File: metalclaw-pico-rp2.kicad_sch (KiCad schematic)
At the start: 124 parts, among them J1 USB4105-GF-A, J2 FTSH-105-01-L-DV-K, SW1 PTS810SJM250SMTR LFS, SW2 PTS810SJM250SMTR LFS, U1 XC6220B331MR-G, U2 RP2354B, U3 APS6404L-3SQR-SN, Y1 ABM8-272-T3

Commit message: Add test points for usb and debugger
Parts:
- added TP1, TP2, TP3, TP4, TP5, TP6, TP7, TP8: TestPoint, TestPoint:TestPoint_Pad_D1.0mm, symbol Connector:TestPoint
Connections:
- net +3V3: now also TP5.1
- net BOOTSEL: now also TP8.1
- net GND: now also TP6.1
- net RESET: now also TP7.1
- net USB_D+: now also TP2.1
- net USB_D-: now also TP1.1
- net at J2.4 (Pin_4), U2.33 (SWCLK): now also TP3.1
- net at J2.2 (Pin_2), U2.34 (SWDIO): now also TP4.1

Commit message: Fix cap value
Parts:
- C11: value 1u -> 4.7u; LCSC C52923 -> C326586; LCSC MPN CL05A105KA5NQNC -> CC0402KRX5R6BB475; Mouser 810-C1005X7S1A105K -> 810-C1005X5R0J475K
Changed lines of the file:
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@@
 			)
 		)
-		(property "Value" "1u"
+		(property "Value" "4.7u"
 			(at 179.578 73.66 90)
 			(effects
@@
 			)
 		)
-		(property "Datasheet" "https://eu.mouser.com/en/ProductDetail/TDK/C1005X7S1A105K050BC"
+		(property "Datasheet" "https://product.tdk.com/en/search/capacitor/ceramic/mlcc/info?part_no=C1005X5R0J475K050BC"
 			(at 177.8 78.74 0)
 			(effects
@@
 			)
 		)
-		(property "Description" "1 uF +/-10% 10 V X7S 0402 carrier MCU decoupling capacitor, TDK C1005X7S1A105K050BC"
+		(property "Description" "4.7 uF 6.3 V X5R +/-10% 0402 regulator input capacitor (CIN), TDK C1005X5R0J475K050BC"
 			(at 177.8 78.74 0)
 			(effects
@@
 			)
 		)
-		(property "Mouser" "810-C1005X7S1A105K"
+		(property "Mouser" "810-C1005X5R0J475K"
 			(at 177.8 78.74 90)
 			(effects
@@
 			)
 		)
-		(property "LCSC" "C52923"
+		(property "LCSC" "C326586"
 			(at 177.8 78.74 90)
 			(effects
@@
 			)
 		)
-		(property "LCSC MPN" "CL05A105KA5NQNC"
+		(property "LCSC MPN" "CC0402KRX5R6BB475"
 			(at 177.8 78.74 90)
 			(effects

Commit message: Update JLCPCB component sourcing and fabrication package
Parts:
- C1, C2: Manufacturer (none) -> Samsung Electro-Mechanics; Mouser 810-C1608X7R1A106M08 -> (none)
- C10, C11, C12, C13, C24: Manufacturer (none) -> Yageo; Mouser 810-C1005X5R0J475K -> (none)
- C14, C15, C16, C17, C18, C19, C20, C21, C22, C23, C25, C29, C3: Manufacturer (none) -> Yageo; Mouser 581-KGM03BR71A104KH -> (none)
- C28: Manufacturer (none) -> Samsung Electro-Mechanics; Mouser 810-C1005X7S1A105K -> (none)
- D1: value CUHS20F30,H3F -> SS14HE; footprint MetalClaw:D_US2H_CUHS20F30 -> MetalClaw:D_SOD-323HE_SS14HE; LCSC C5357828 -> C28646397; MPN (none) -> SS14HE; Manufacturer (none) -> TECH PUBLIC; Mouser 757-CUHS20F30H3F -> (none)
- J1: value USB4105-GF-A -> HH 16P TYPE-C (Y495); footprint MetalClaw:USB_C_Receptacle_GCT_USB4105-xx-A_16P_TopMnt_Horizontal -> MetalClaw:USB_C_Receptacle_HH_Y495_16P_TopMnt_Horizontal; LCSC C3020560 -> C52209111; MPN USB4105-GF-A -> HH 16P TYPE-C (Y495); Manufacturer GCT -> HH; Mouser 640-USB4105-GF-A -> (none); Supplier (none) -> JLCPCB/LCSC
- SW1, SW2: value PTS810SJM250SMTR LFS -> YTS810SJM; LCSC C116501 -> C2910643; MPN (none) -> YTS810SJM; Manufacturer (none) -> YIYUAN; Mouser 611-PTS810SJM250SMTR -> (none)
- U3: MPN (none) -> APS6404L-3SQR-SN; Manufacturer (none) -> AP Memory; Mouser 878-APS6404L-3SQR-SN -> (none)

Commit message: Correct assembly footprints and prepare JLCPCB manufacturing package
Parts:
- J2: footprint Connector_PinHeader_1.27mm:PinHeader_2x05_P1.27mm_Vertical_SMD -> MetalClaw:Samtec_FTSH-105-01-L-DV-K
- L1: footprint Inductor_SMD_Wurth:L_Wurth_WE-LQSH-2010 -> MetalClaw:L_Abracon_AOTA-B201610S3R3-101-T
- U2: footprint Package_DFN_QFN:QFN-80-1EP_10x10mm_P0.4mm_EP3.4x3.4mm -> MetalClaw:QFN-80_RP2354B_10x10mm_P0.4mm_EP3.4mm_ViaAwarePaste
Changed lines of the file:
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@@
 			)
 		)
-		(property "Footprint" "Package_DFN_QFN:QFN-80-1EP_10x10mm_P0.4mm_EP3.4x3.4mm"
+		(property "Footprint" "MetalClaw:QFN-80_RP2354B_10x10mm_P0.4mm_EP3.4mm_ViaAwarePaste"
 			(at 295.91 146.05 0)
 			(effects
@@
 			)
 		)
-		(property "Footprint" "Inductor_SMD_Wurth:L_Wurth_WE-LQSH-2010"
+		(property "Footprint" "MetalClaw:L_Abracon_AOTA-B201610S3R3-101-T"
 			(at 290.83 80.01 0)
 			(effects
@@
 			)
 		)
-		(property "Footprint" "Connector_PinHeader_1.27mm:PinHeader_2x05_P1.27mm_Vertical_SMD"
+		(property "Footprint" "MetalClaw:Samtec_FTSH-105-01-L-DV-K"
 			(at 375.92 187.96 0)
 			(effects

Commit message: Prepare v1.r1 documentation and release workflow
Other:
- title: (none) -> MetalClaw Pico RP2
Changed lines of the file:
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@@
 	(generator_version "9.0")
 	(paper "B")
+	(title_block
+		(title "MetalClaw Pico RP2")
+		(date "2026-10-24")
+		(rev "v1.r1")
+		(comment 1 "Author: Renz Bagaporo")
+	)
 	(junction
 		(at 252.73 97.79)

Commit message: Select compact keyed Samtec SWD header for JLCPCB assembly
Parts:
- J2: value FTSH-105-01-L-DV-K -> FTSH-105-01-L-DV-K-P-TR; LCSC C5155080 -> C2932107; MPN FTSH-105-01-L-DV-K -> FTSH-105-01-L-DV-K-P-TR; Mouser 200-FTSH10501LDVK -> (none)
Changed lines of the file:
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@@
 			)
 		)
-		(property "Value" "FTSH-105-01-L-DV-K"
+		(property "Value" "FTSH-105-01-L-DV-K-P-TR"
 			(at 377.19 198.628 0)
 			(effects
@@
 			)
 		)
-		(property "Datasheet" "https://www.samtec.com/products/ftsh-105-01-l-dv-k"
+		(property "Datasheet" "https://suddendocs.samtec.com/prints/ftsh-1xx-xx-xxx-dv-xxx-xxx-mkt.pdf"
 			(at 375.92 187.96 0)
 			(effects
@@
 			)
 		)
-		(property "Description" "10-pin 2-row 1.27 mm vertical SMT micro header with keying notch for SWD, Samtec FTSH-105-01-L-DV-K"
+		(property "Description" "10-pin 2-row 1.27 mm vertical SMT SWD header with compact plastic key, 3.05 mm mating posts, 10 microinch gold / matte tin, pick-and-place pad, tape and reel; Samtec FTSH-105-01-L-DV-K-P-TR"
 			(at 375.92 187.96 0)
 			(effects
@@
 			)
 		)
-		(property "MPN" "FTSH-105-01-L-DV-K"
+		(property "MPN" "FTSH-105-01-L-DV-K-P-TR"
 			(at 375.92 187.96 0)
 			(effects
@@
 			)
 		)
-		(property "Mouser" "200-FTSH10501LDVK"
+		(property "Mouser" ""
 			(at 375.92 187.96 0)
 			(effects
@@
 			)
 		)
-		(property "LCSC" "C5155080"
+		(property "LCSC" "C2932107"
 			(at 375.92 187.96 0)
 			(effects

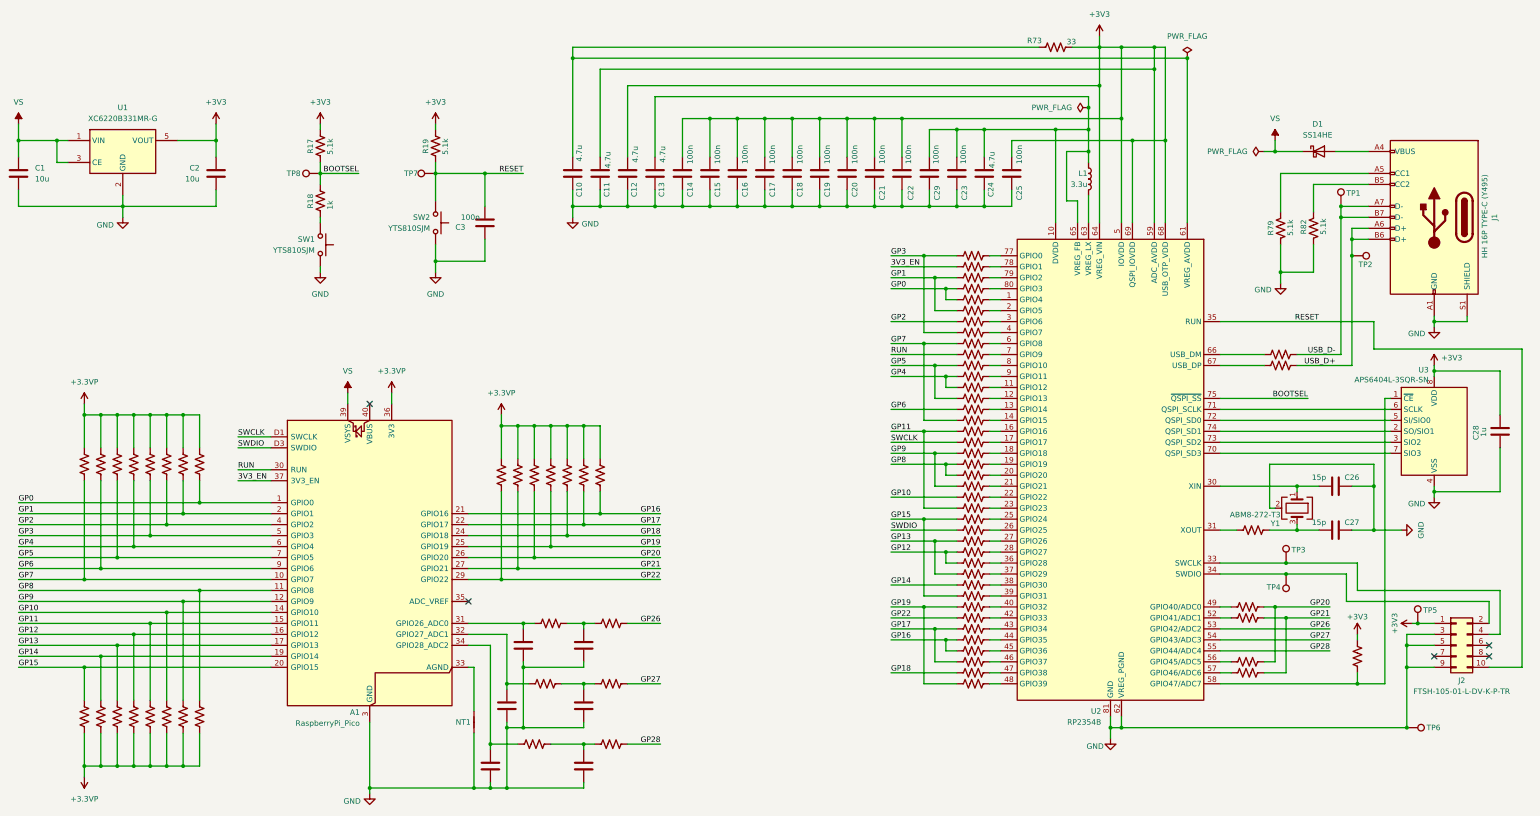
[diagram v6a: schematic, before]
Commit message: Reduce assembly BOM cost and add unshrouded SWD orientation outline
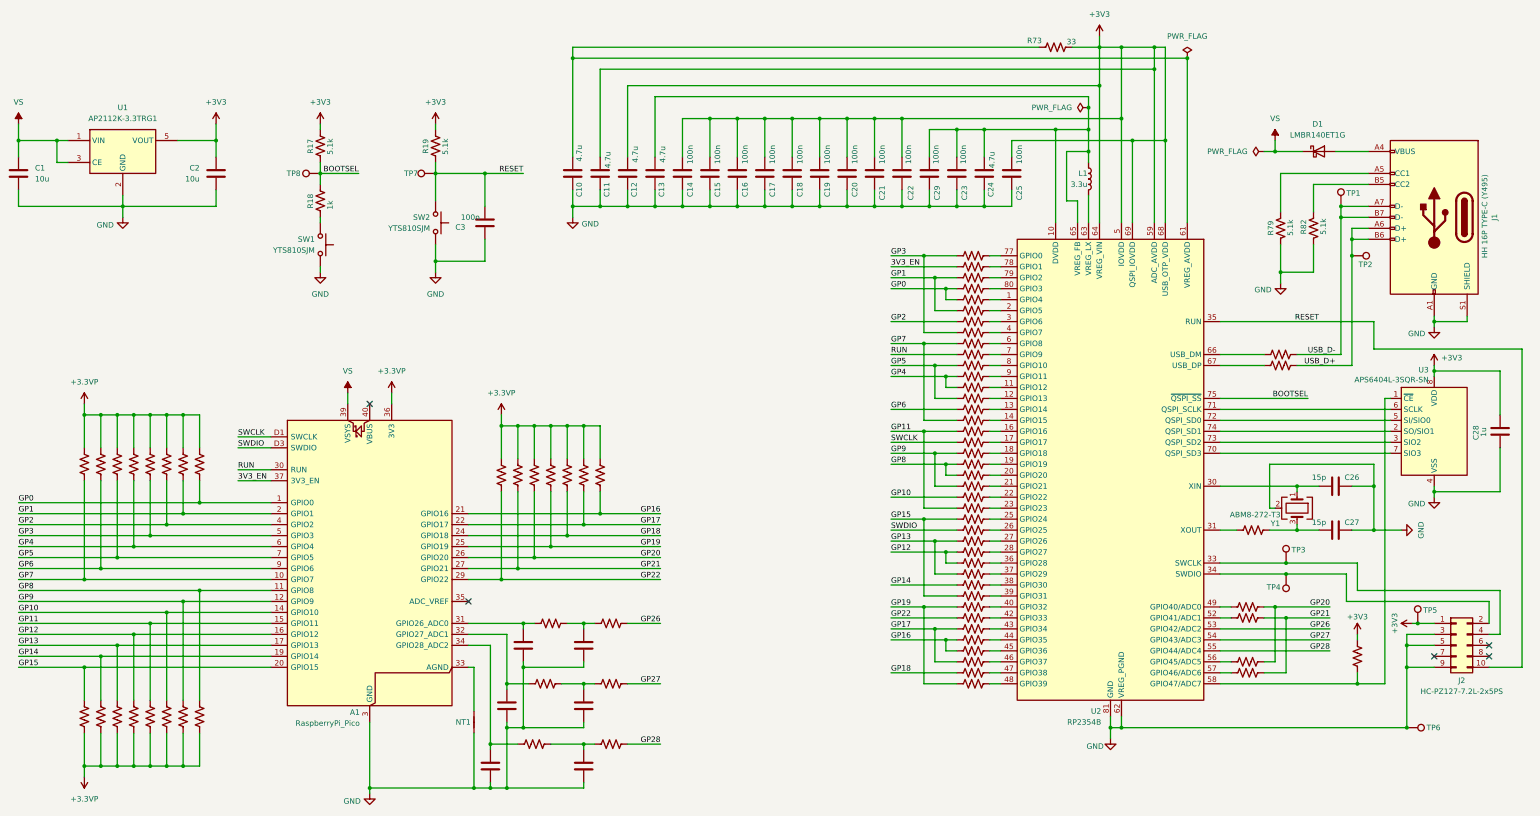
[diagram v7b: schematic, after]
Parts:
- D1: value SS14HE -> LMBR140ET1G; LCSC C28646397 -> C172430; MPN SS14HE -> LMBR140ET1G; Manufacturer TECH PUBLIC -> LRC
- J2: value FTSH-105-01-L-DV-K-P-TR -> HC-PZ127-7.2L-2x5PS; footprint MetalClaw:Samtec_FTSH-105-01-L-DV-K -> MetalClaw:HCTL_HC-PZ127-7.2L-2x5PS; LCSC C2932107 -> C27985146; MPN FTSH-105-01-L-DV-K-P-TR -> HC-PZ127-7.2L-2x5PS; Manufacturer Samtec -> HCTL
- U1: value XC6220B331MR-G -> AP2112K-3.3TRG1; LCSC C86534 -> C51118; MPN (none) -> AP2112K-3.3TRG1; Manufacturer (none) -> Diodes Incorporated; Mouser 865-XC6220B331MR-G -> (none)
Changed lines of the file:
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@@
 			)
 		)
-		(property "Value" "XC6220B331MR-G"
+		(property "Value" "AP2112K-3.3TRG1"
 			(at 67.31 66.04 0)
 			(effects
@@
 			)
 		)
-		(property "Datasheet" "https://www.torexsemi.com/file/xc6220/XC6220.pdf"
+		(property "Datasheet" "https://www.diodes.com/datasheet/download/AP2112.pdf"
 			(at 86.36 99.06 0)
 			(effects
@@
 			)
 		)
-		(property "Description" "1 A low-dropout regulator, fixed 3.3 V output, SOT-25, Torex XC6220B331MR-G"
+		(property "Description" "600 mA fixed 3.3 V low-dropout regulator, SOT-25, active-high enable; Diodes Incorporated AP2112K-3.3TRG1"
 			(at 67.31 73.66 0)
 			(effects
@@
 			)
 		)
-		(property "Mouser" "865-XC6220B331MR-G"
+		(property "Mouser" ""
+			(at 67.31 73.66 0)
+			(effects
+				(font
+					(size 1.27 1.27)
+				)
+				(hide yes)
+			)
+		)
+		(property "Manufacturer" "Diodes Incorporated"
+			(at 67.31 73.66 0)
+			(effects
+				(font
+					(size 1.27 1.27)
+				)
+				(hide yes)
+			)
+		)
+		(property "MPN" "AP2112K-3.3TRG1"
 			(at 67.31 73.66 0)
 			(effects
@@
 			)
 		)
-		(property "LCSC" "C86534"
+		(property "LCSC" "C51118"
 			(at 67.31 73.66 0)
 			(effects
@@
 			)
 		)
-		(property "Value" "FTSH-105-01-L-DV-K-P-TR"
+		(property "Value" "HC-PZ127-7.2L-2x5PS"
 			(at 377.19 198.628 0)
 			(effects
@@
 			)
 		)
-		(property "Footprint" "MetalClaw:Samtec_FTSH-105-01-L-DV-K"
+		(property "Footprint" "MetalClaw:HCTL_HC-PZ127-7.2L-2x5PS"
 			(at 375.92 187.96 0)
 			(effects
@@
 			)
 		)
-		(property "Datasheet" "https://suddendocs.samtec.com/prints/ftsh-1xx-xx-xxx-dv-xxx-xxx-mkt.pdf"
+		(property "Datasheet" "https://datasheet.lcsc.com/datasheet/pdf/6cceb9a5157e418f0d202dde8ff2fbeb.pdf?productCode=C27985146"
 			(at 375.92 187.96 0)
 			(effects
@@
 			)
 		)
-		(property "Description" "10-pin 2-row 1.27 mm vertical SMT SWD header with compact plastic key, 3.05 mm mating posts, 10 microinch gold / matte tin, pick-and-place pad, tape and reel; Samtec FTSH-105-01-L-DV-K-P-TR"
+		(property "Description" "10-pin 2-row 1.27 mm vertical SMT unshrouded header, 0.40 mm square contacts, 4.0 mm mating posts; HCTL HC-PZ127-7.2L-2x5PS"
 			(at 375.92 187.96 0)
 			(effects
@@
 			)
 		)
-		(property "Manufacturer" "Samtec"
+		(property "Manufacturer" "HCTL"
 			(at 375.92 187.96 0)
 			(effects
@@
 			)
 		)
-		(property "MPN" "FTSH-105-01-L-DV-K-P-TR"
+		(property "MPN" "HC-PZ127-7.2L-2x5PS"
 			(at 375.92 187.96 0)
 			(effects
@@
 			)
 		)
-		(property "LCSC" "C2932107"
+		(property "LCSC" "C27985146"
 			(at 375.92 187.96 0)
 			(effects
@@
 			)
 		)
-		(property "Value" "SS14HE"
+		(property "Value" "LMBR140ET1G"
 			(at 343.8525 69.85 0)
 			(effects
@@
 			)
 		)
-		(property "Datasheet" "https://datasheet.lcsc.com/datasheet/pdf/6c23897d9338a6092c7736bca8f498a2.pdf?productCode=C28646397"
+		(property "Datasheet" "https://www.lrc.cn/Upload/PDF/Product/SBD/LMBR140ET1G.pdf"
 			(at 344.17 73.66 0)
 			(effects
@@
 			)
 		)
-		(property "Description" "40 V 1 A Schottky barrier diode, SOD-323HE, TECH PUBLIC SS14HE"
+		(property "Description" "40 V 1 A Schottky barrier diode, SOD-323HE, large underside cathode; LRC LMBR140ET1G"
 			(at 344.17 73.66 0)
 			(effects
@@
 			)
 		)
-		(property "Manufacturer" "TECH PUBLIC"
+		(property "Manufacturer" "LRC"
 			(at 344.17 73.66 0)
 			(effects
@@
 			)
 		)
-		(property "LCSC" "C28646397"
+		(property "LCSC" "C172430"
 			(at 344.17 73.66 0)
 			(effects
@@
 			)
 		)
-		(property "MPN" "SS14HE"
+		(property "MPN" "LMBR140ET1G"
 			(at 344.17 73.66 0)
 			(effects

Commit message: Qualify regulator capacitors and finalize prototype release sourcing
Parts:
- C10, C11, C12, C13, C24: LCSC C326586 -> C82453; LCSC MPN CC0402KRX5R6BB475 -> GRM155R60J475ME47D; MPN (none) -> GRM155R60J475ME47D; Manufacturer Yageo -> Murata
- R80, R81: LCSC C273268 -> C367568; MPN (none) -> WR02X27R0FAL; Manufacturer (none) -> Walsin; Mouser 603-RC0201FR-0727RL -> (none)
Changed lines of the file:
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@@
 			)
 		)
-		(property "Datasheet" "https://yageogroup.com/download/specsheet/CC0402KRX5R6BB475"
+		(property "Datasheet" "https://search.murata.co.jp/Ceramy/image/img/A01X/G101/ENG/GRM155R60J475ME47-17A.pdf"
 			(at 177.8 78.74 0)
 			(effects
@@
 			)
 		)
-		(property "Description" "4.7 uF 10 V X5R +/-10% 0402 regulator input capacitor (CIN), Yageo CC0402KRX5R6BB475"
+		(property "Description" "4.7 uF 6.3 V X5R +/-20% 0402 regulator input capacitor (CIN), Murata GRM155R60J475ME47D"
 			(at 177.8 78.74 0)
 			(effects
@@
 			)
 		)
-		(property "Manufacturer" "Yageo"
+		(property "Manufacturer" "Murata"
+			(at 177.8 78.74 90)
+			(effects
+				(font
+					(size 1.27 1.27)
+				)
+				(hide yes)
+			)
+		)
+		(property "MPN" "GRM155R60J475ME47D"
 			(at 177.8 78.74 90)
 			(effects
@@
 			)
 		)
-		(property "LCSC" "C326586"
+		(property "LCSC" "C82453"
 			(at 177.8 78.74 90)
 			(effects
@@
 			)
 		)
-		(property "LCSC MPN" "CC0402KRX5R6BB475"
+		(property "LCSC MPN" "GRM155R60J475ME47D"
 			(at 177.8 78.74 90)
 			(effects
@@
 			)
 		)
-		(property "Datasheet" "https://www.mouser.com/ProductDetail/YAGEO/RC0201FR-0727RL"
+		(property "Datasheet" "https://www.mouser.com/ds/2/210/WR02X-247974.pdf"
 			(at 335.28 123.19 0)
 			(effects
@@
 			)
 		)
-		(property "Description" "27 ohm +/-1% 1/20 W 0201 USB data series resistor, Yageo RC0201FR-0727RL"
+		(property "Description" "27 ohm +/-1% 50 mW 0201 USB data series resistor, Walsin WR02X27R0FAL"
 			(at 335.28 123.19 0)
 			(effects
@@
 			)
 		)
-		(property "Mouser" "603-RC0201FR-0727RL"
+		(property "Mouser" ""
+			(at 335.28 123.19 90)
+			(effects
+				(font
+					(size 1.27 1.27)
+				)
+				(hide yes)
+			)
+		)
+		(property "Manufacturer" "Walsin"
+			(at 335.28 123.19 90)
+			(effects
+				(font
+					(size 1.27 1.27)
+				)
+				(hide yes)
+			)
+		)
+		(property "MPN" "WR02X27R0FAL"
 			(at 335.28 123.19 90)
 			(effects
@@
 			)
 		)
-		(property "LCSC" "C273268"
+		(property "LCSC" "C367568"
 			(at 335.28 123.19 90)
 			(effects
@@
 			)
 		)
-		(property "Datasheet" "https://www.mouser.com/ProductDetail/YAGEO/RC0201FR-0727RL"
+		(property "Datasheet" "https://www.mouser.com/ds/2/210/WR02X-247974.pdf"
 			(at 335.28 120.65 0)
 			(effects
@@
 			)
 		)
-		(property "Description" "27 ohm +/-1% 1/20 W 0201 USB data series resistor, Yageo RC0201FR-0727RL"
+		(property "Description" "27 ohm +/-1% 50 mW 0201 USB data series resistor, Walsin WR02X27R0FAL"
 			(at 335.28 120.65 0)
 			(effects
@@
 			)
 		)
-		(property "Mouser" "603-RC0201FR-0727RL"
+		(property "Mouser" ""
+			(at 335.28 120.65 90)
+			(effects
+				(font
+					(size 1.27 1.27)
+				)
+				(hide yes)
+			)
+		)
+		(property "Manufacturer" "Walsin"
 			(at 335.28 120.65 90)
 			(effects
@@
 			)
 		)
-		(property "LCSC" "C273268"
+		(property "MPN" "WR02X27R0FAL"
+			(at 335.28 120.65 90)
+			(effects
+				(font
+					(size 1.27 1.27)
+				)
+				(hide yes)
+			)
+		)
+		(property "LCSC" "C367568"
 			(at 335.28 120.65 90)
 			(effects
@@
 			)
 		)
-		(property "Datasheet" "https://yageogroup.com/download/specsheet/CC0402KRX5R6BB475"
+		(property "Datasheet" "https://search.murata.co.jp/Ceramy/image/img/A01X/G101/ENG/GRM155R60J475ME47-17A.pdf"
 			(at 184.15 78.74 0)
 			(effects
@@
 			)
 		)
-		(property "Description" "4.7 uF 10 V X5R +/-10% 0402 MLCC, Yageo CC0402KRX5R6BB475"
+		(property "Description" "4.7 uF 6.3 V X5R +/-20% 0402 MLCC, Murata GRM155R60J475ME47D"
 			(at 184.15 78.74 0)
 			(effects
@@
 			)
 		)
-		(property "Manufacturer" "Yageo"
+		(property "Manufacturer" "Murata"
+			(at 184.15 78.74 90)
+			(effects
+				(font
+					(size 1.27 1.27)
+				)
+				(hide yes)
+			)
+		)
+		(property "MPN" "GRM155R60J475ME47D"
 			(at 184.15 78.74 90)
 			(effects
@@
 			)
 		)
-		(property "LCSC" "C326586"
+		(property "LCSC" "C82453"
 			(at 184.15 78.74 90)
 			(effects
@@
 			)
 		)
-		(property "LCSC MPN" "CC0402KRX5R6BB475"
+		(property "LCSC MPN" "GRM155R60J475ME47D"
 			(at 184.15 78.74 90)
 			(effects
@@
 			)
 		)
-		(property "Datasheet" "https://yageogroup.com/download/specsheet/CC0402KRX5R6BB475"
+		(property "Datasheet" "https://search.murata.co.jp/Ceramy/image/img/A01X/G101/ENG/GRM155R60J475ME47-17A.pdf"
 			(at 171.45 78.74 0)
 			(effects
@@
 			)
 		)
-		(property "Description" "4.7 uF 10 V X5R +/-10% 0402 VREG_AVDD filter capacitor, Yageo CC0402KRX5R6BB475"
+		(property "Description" "4.7 uF 6.3 V X5R +/-20% 0402 VREG_AVDD filter capacitor, Murata GRM155R60J475ME47D"
 			(at 171.45 78.74 0)
 			(effects
@@
 			)
 		)
-		(property "Manufacturer" "Yageo"
+		(property "Manufacturer" "Murata"
 			(at 171.45 78.74 90)
 			(effects
@@
 			)
 		)
-		(property "LCSC" "C326586"
+		(property "MPN" "GRM155R60J475ME47D"
 			(at 171.45 78.74 90)
 			(effects
@@
 			)
 		)
-		(property "LCSC MPN" "CC0402KRX5R6BB475"
+		(property "LCSC" "C82453"
+			(at 171.45 78.74 90)
+			(effects
+				(font
+					(size 1.27 1.27)
+				)
+				(hide yes)
+			)
+		)
+		(property "LCSC MPN" "GRM155R60J475ME47D"
 			(at 171.45 78.74 90)
 			(effects
@@
 			)
 		)
-		(property "Datasheet" "https://yageogroup.com/download/specsheet/CC0402KRX5R6BB475"
+		(property "Datasheet" "https://search.murata.co.jp/Ceramy/image/img/A01X/G101/ENG/GRM155R60J475ME47-17A.pdf"
 			(at 266.7 78.74 0)
 			(effects
@@
 			)
 		)
-		(property "Description" "4.7 uF 10 V X5R +/-10% 0402 MLCC, Yageo CC0402KRX5R6BB475"
+		(property "Description" "4.7 uF 6.3 V X5R +/-20% 0402 MLCC, Murata GRM155R60J475ME47D"
 			(at 266.7 78.74 0)
 			(effects
@@
 			)
 		)
-		(property "Manufacturer" "Yageo"
+		(property "Manufacturer" "Murata"
+			(at 266.7 78.74 90)
+			(effects
+				(font
+					(size 1.27 1.27)
+				)
+				(hide yes)
+			)
+		)
+		(property "MPN" "GRM155R60J475ME47D"
 			(at 266.7 78.74 90)
 			(effects
@@
 			)
 		)
-		(property "LCSC" "C326586"
+		(property "LCSC" "C82453"
 			(at 266.7 78.74 90)
 			(effects
@@
 			)
 		)
-		(property "LCSC MPN" "CC0402KRX5R6BB475"
+		(property "LCSC MPN" "GRM155R60J475ME47D"
 			(at 266.7 78.74 90)
 			(effects
@@
 			)
 		)
-		(property "Datasheet" "https://yageogroup.com/download/specsheet/CC0402KRX5R6BB475"
+		(property "Datasheet" "https://search.murata.co.jp/Ceramy/image/img/A01X/G101/ENG/GRM155R60J475ME47-17A.pdf"
 			(at 190.5 78.74 0)
 			(effects
@@
 			)
 		)
-		(property "Description" "4.7 uF 10 V X5R +/-10% 0402 MLCC, Yageo CC0402KRX5R6BB475"
+		(property "Description" "4.7 uF 6.3 V X5R +/-20% 0402 MLCC, Murata GRM155R60J475ME47D"
 			(at 190.5 78.74 0)
 			(effects
@@
 			)
 		)
-		(property "Manufacturer" "Yageo"
+		(property "Manufacturer" "Murata"
+			(at 190.5 78.74 90)
+			(effects
+				(font
+					(size 1.27 1.27)
+				)
+				(hide yes)
+			)
+		)
+		(property "MPN" "GRM155R60J475ME47D"
 			(at 190.5 78.74 90)
 			(effects
@@
 			)
 		)
-		(property "LCSC" "C326586"
+		(property "LCSC" "C82453"
 			(at 190.5 78.74 90)
 			(effects
@@
 			)
 		)
-		(property "LCSC MPN" "CC0402KRX5R6BB475"
+		(property "LCSC MPN" "GRM155R60J475ME47D"
 			(at 190.5 78.74 90)
 			(effects
